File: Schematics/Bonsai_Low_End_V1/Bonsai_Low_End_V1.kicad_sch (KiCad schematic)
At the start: 6 parts, among them U1 MOUDLE-SEEEDUINO-XIAO-ESP32C3, U2 MAX30101EFD

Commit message: Before Everything Breaks
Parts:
- removed C2: 10uF, symbol Device:C_Small
- added C3: 1.0uF, symbol Device:C_Small
- added C5: 10uF, symbol Device:C_Small
- added D1: RED, symbol Device:LED
- added J1: Conn_01x02_Socket, symbol Connector:Conn_01x02_Socket
- added R3: 2,2k, symbol Device:R_Small
- added R4, R7, R8: 4.7k, symbol Device:R_Small
- added R4, R5, R6: 2.2k, symbol Device:R_Small
- added U3, U4: RE1C002UN, RE1C002UN:EMT3F, symbol RE1C002UN:RE1C002UN
- added U5: DRV2605LDGS, Package_SO:VSSOP-10_3x3mm_P0.5mm, symbol Driver_Haptic:DRV2605LDGS
- U1: footprint MOUDLE14P-SMD-2.54-21X17.8MM -> xiao ESP32C3_PCB:MOUDLE14P-SMD-2.54-21X17.8MM
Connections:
- net GND2 is gone; now on net GND: U2.4 (PGND)
- net +1V8: now also R1.1, R3.1, U3.P$1, U4.P$1
- net +5V: now also C5.1
- net GND: now also U1.13 (GND), C3.2, C5.2, R7.2, R8.2, U5.4 (IN/TRIG), U5.8 (GND)
- net LV_SCL: now also R1.2, U3.P$2
- net LV_SDA: now also R3.2, U4.P$2
- net SCL: now also R2.2, U1.6 (PA9_A5_D5_SCL), R6.1, U3.P$3, U5.2 (SCL); no longer U1.5 (PA8_A4_D4_SDA)
- net SDA: now also U1.5 (PA8_A4_D4_SDA), R4.2, R5.1, U4.P$3, U5.3 (SDA); no longer U1.6 (PA9_A5_D5_SCL)
- net +3V3: now reaches R2.1
- net +3V3: now also U1.12 (3V3), R4.1, R4.1, R5.2, R6.2
- net HapticEN: now reaches U1.10 (PA5_A9_D9_MISO)
- net HapticEN: now also R8.1, U5.5 (EN)
- net at U1.11 (PA6_A10_D10_MOSI): now also D1.2 (A)
- net VCC: now reaches U1.14 (5V)
- net VCC: now also U5.10 (VDD), U5.6 (VDD/NC)
- net !INT: no longer names the net of U2.13 (~{INT})
- net !INT: now also R4.2
- new net: D1.1 (K), R7.1
- new net: C3.1, U5.1 (REG)
- new net: J1.1 (Pin_1), U5.7 (OUT+)
- new net: J1.2 (Pin_2), U5.9 (OUT-)
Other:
- moved on the sheet: C1, R1, R2, U1, U2

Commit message: Added Driver and Haptic Motor
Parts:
- removed J1: Conn_01x02_Socket, symbol Connector:Conn_01x02_Socket
- removed R4: 4.7k, symbol Device:R_Small
- added R9: 2.2k, symbol Device:R_Small
- added U6: ~, BonsaiFootPrintLib:VLV101040A, symbol Custom_Symbols_Bonsai:VLV101040A
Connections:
- net +3V3: now also R9.1
- net at U5.7 (OUT+): now also U6.1 (VCC)
- net at U5.9 (OUT-): now also U6.2 (GND)
- net at U2.13 (~{INT}): now also R9.2
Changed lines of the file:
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@@
+    (effects (font (size 1.27 1.27)) (justify left bottom))
+  )
+  (label "Driver and Haptic Motor" (at 142.24 81.28 0) (fields_autoplaced)
     (effects (font (size 1.27 1.27)) (justify left bottom))
   )
@@
     )
   )
+  (symbol (lib_id "Custom_Symbols_Bonsai:VLV101040A") (at 185.42 99.06 0) (unit 1)
+    (in_bom yes) (on_board yes) (dnp no) (fields_autoplaced)
+    (property "Reference" "U6" (at 189.23 100.33 0)
+      (effects (font (size 1.27 1.27)) (justify left))
+    )
+    (property "Value" "~" (at 185.42 99.06 0)
+      (effects (font (size 1.27 1.27)))
+    )
+    (property "Footprint" "BonsaiFootPrintLib:VLV101040A" (at 185.42 99.06 0)
+      (effects (font (size 1.27 1.27)) hide)
+    )
+    (property "Datasheet" "" (at 185.42 99.06 0)
+      (effects (font (size 1.27 1.27)) hide)
+    )
+    (pin "1")
+    (pin "2")
+    (instances
+      (project "Bonsai_Low_End_V1"
+        (path "/b393c629-c38d-42fe-a79b-f8ec17a7bd02"
+          (reference "U6") (unit 1)
+        )
+      )
+    )
+  )
   (symbol (lib_id "Device:R_Small") (at 152.4 118.11 0) (unit 1)
     (in_bom yes) (on_board yes) (dnp no)
@@
     )
   )
-  (symbol (lib_id "Connector:Conn_01x02_Socket") (at 189.23 95.25 0) (unit 1)
-    (in_bom yes) (on_board yes) (dnp no)
-    (property "Reference" "J1" (at 190.5 90.17 0)
-      (effects (font (size 1.27 1.27)) (justify left))
-    )
-    (property "Value" "Conn_01x02_Socket" (at 190.5 92.71 0)
-      (effects (font (size 1.27 1.27)) (justify left))
-    )
-    (property "Footprint" "" (at 189.23 95.25 0)
-      (effects (font (size 1.27 1.27)) hide)
-    )
-    (property "Datasheet" "~" (at 189.23 95.25 0)
-      (effects (font (size 1.27 1.27)) hide)
-    )
-    (pin "1")
-    (pin "2")
-    (instances
-      (project "Bonsai_Low_End_V1"
-        (path "/b393c629-c38d-42fe-a79b-f8ec17a7bd02"
-          (reference "J1") (unit 1)
-        )
-      )
-    )
-  )
   (symbol (lib_id "power:+5V") (at 151.13 44.45 0) (unit 1)
     (in_bom yes) (on_board yes) (dnp no)
@@
         (path "/b393c629-c38d-42fe-a79b-f8ec17a7bd02"
           (reference "#PWR011") (unit 1)
-        )
-      )
-    )
-  )
-  (symbol (lib_id "Device:R_Small") (at 184.15 22.86 0) (unit 1)
-    (in_bom yes) (on_board yes) (dnp no) (fields_autoplaced)
-    (property "Reference" "R4" (at 186.69 21.59 0)
-      (effects (font (size 1.27 1.27)) (justify left))
-    )
-    (property "Value" "4.7k" (at 186.69 24.13 0)
-      (effects (font (size 1.27 1.27)) (justify left))
-    )
-    (property "Footprint" "" (at 184.15 22.86 0)
-      (effects (font (size 1.27 1.27)) hide)
-    )
-    (property "Datasheet" "~" (at 184.15 22.86 0)
-      (effects (font (size 1.27 1.27)) hide)
-    )
-    (pin "1")
-    (pin "2")
-    (instances
-      (project "Bonsai_Low_End_V1"
-        (path "/b393c629-c38d-42fe-a79b-f8ec17a7bd02"
-          (reference "R4") (unit 1)
         )
       )
@@
         )
       )
+    )
+  )
+  (symbol (lib_id "Device:R_Small") (at 184.15 22.86 0) (unit 1)
+    (in_bom yes) (on_board yes) (dnp no) (fields_autoplaced)
+    (property "Reference" "R9" (at 186.69 21.59 0)
+      (effects (font (size 1.27 1.27)) (justify left))
+    )
+    (property "Value" "2.2k" (at 186.69 24.13 0)
+      (effects (font (size 1.27 1.27)) (justify left))
+    )
+    (property "Footprint" "" (at 184.15 22.86 0)
+      (effects (font (size 1.27 1.27)) hide)
+    )
+    (property "Datasheet" "~" (at 184.15 22.86 0)
+      (effects (font (size 1.27 1.27)) hide)
+    )
+    (pin "1")
+    (pin "2")
+    (instances
+      (project "Bonsai_Low_End_V1"
+        (path "/b393c629-c38d-42fe-a79b-f8ec17a7bd02"
+          (reference "R9") (unit 1)
+        )
+      )

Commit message: last psuh before feedback
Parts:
- removed R3: 2,2k, symbol Device:R_Small
- removed R4: 2.2k, symbol Device:R_Small
- removed U4: RE1C002UN, RE1C002UN:EMT3F, symbol RE1C002UN:RE1C002UN
- added U7: RE1C002UN, RE1C002UN:EMT3F, symbol RE1C002UN:RE1C002UN
- C5: value 10uF -> 50uF
- R2: value 2.2k -> 2,2k
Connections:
- net +1V8: now also R2.1, U7.P$1
- net +3V3: no longer R2.1
- net +5V: no longer C5.1
- net LV_SDA: now also R2.2, U7.P$2
- net SCL: no longer R2.2
- net SDA: now also U7.P$3
- net VCC: now also C5.1
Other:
- company: (none) -> Bonsai
- title: (none) -> Bonsai Wearable Prototype
- moved on the sheet: C1, C3, C5, D1, R1, R5, R6, R7, R8, R9, U1, U2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

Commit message: Made PCB
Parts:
- C1, C3: footprint (none) -> Capacitor_SMD:C_0603_1608Metric_Pad1.08x0.95mm_HandSolder
- C5: footprint (none) -> Capacitor_SMD:C_0805_2012Metric_Pad1.18x1.45mm_HandSolder
- D1: footprint (none) -> LED_SMD:LED_0603_1608Metric_Pad1.05x0.95mm_HandSolder
- R1, R2, R5, R6, R7, R8, R9: footprint (none) -> Resistor_SMD:R_0603_1608Metric_Pad0.98x0.95mm_HandSolder
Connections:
- net HapticEN: now also U1.3 (PA10_A2_D2); no longer U1.10 (PA5_A9_D9_MISO)
- net at U1.11 (PA6_A10_D10_MOSI): no longer D1.2 (A)
- net FUN_LIGHT: now reaches U1.7 (PB08_A6_D6_TX)
- net FUN_LIGHT: now also D1.2 (A)
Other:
- moved on the sheet: C1, C3, C5, D1, R1, R2, R5, R6, R7, R8, R9, U1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

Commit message: Improved
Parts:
- removed U3, U7: RE1C002UN, RE1C002UN:EMT3F, symbol RE1C002UN:RE1C002UN
- added C2: 1uF, Capacitor_SMD:C_0805_2012Metric_Pad1.18x1.45mm_HandSolder, symbol Device:C_Small
- added D2: D_Small_Filled, symbol Device:D_Small_Filled
- added J1: Bat_Connector, Connector_JST:JST_EH_B2B-EH-A_1x02_P2.50mm_Vertical, symbol PCM_SL_Connectors:JST_02
- added Q1: PMOS, symbol Simulation_SPICE:PMOS
- added R3: 2.2k, Resistor_SMD:R_0603_1608Metric_Pad0.98x0.95mm_HandSolder, symbol Device:R_Small
- added R4: 4.7k, Resistor_SMD:R_0603_1608Metric_Pad0.98x0.95mm_HandSolder, symbol Device:R_Small
- added U3: 1.8V, Package_TO_SOT_SMD:SOT-23-5, symbol Regulator_Linear:AP2204K-1.8
- R1: value 2,2k -> 4.7k
- R2: value 2,2k -> 2.2k
- R5: value 2.2k -> 4.7k
- R6, R9: value 2.2k -> 220k
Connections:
- net +5V is gone; now on net VCC: U2.10 (VLED+), U2.9 (VLED+)
- net +1V8: now also U3.5 (VOUT); no longer R1.1, R2.1
- net +3V3: now also R2.2, R3.2; no longer R5.2, R6.2, R9.1
- net GND: now also R1.2, R5.2, C2.2, U3.2 (GND); no longer U5.4 (IN/TRIG)
- net HapticEN: now also U1.2 (PA4_A1_D1); no longer U1.3 (PA10_A2_D2)
- net SCL: now also U2.2 (SCL), R3.1; no longer R6.1
- net SDA: now also R2.1, U2.3 (SDA); no longer R5.1
- net VCC: now also C2.1, R4.2, U3.1 (VIN)
- net Bat_Ind: now reaches R9.2
- net Bat_Ind: now also U1.11 (PA6_A10_D10_MOSI), Q1.1 (D); no longer U2.13 (~{INT})
- net DRV_IN/TRIG: now reaches U1.10 (PA5_A9_D9_MISO)
- net DRV_IN/TRIG: now also R5.1, U5.4 (IN/TRIG)
- net Bat_Ind_EN: now reaches U1.4 (PA11_A3_D3)
- net Bat_Ind_EN: now also Q1.2 (G)
- net INT MAX: now reaches U1.8 (PB09_A7_D7_RX)
- net INT MAX: now also U2.13 (~{INT}), R4.1
- removed net LV_SCL: R1.2, U2.2 (SCL)
- removed net LV_SDA: R2.2, U2.3 (SDA)
- new net: Q1.3 (S), R6.2
- new net: R1.1, U3.3 (EN)
- new net: D2.2 (A), J1.1
- new net Bat+: D2.1 (K), R6.1, U1.15 (Bat+)
- new net Bat-: J1.2, R9.1, U1.16 (Bat-)
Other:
- note added: "Battery Stuff"
- note added: "NOT TO BE USED AS VCC!"
- moved on the sheet: C3, C5, D1, R7, R8, U2, U5, U6

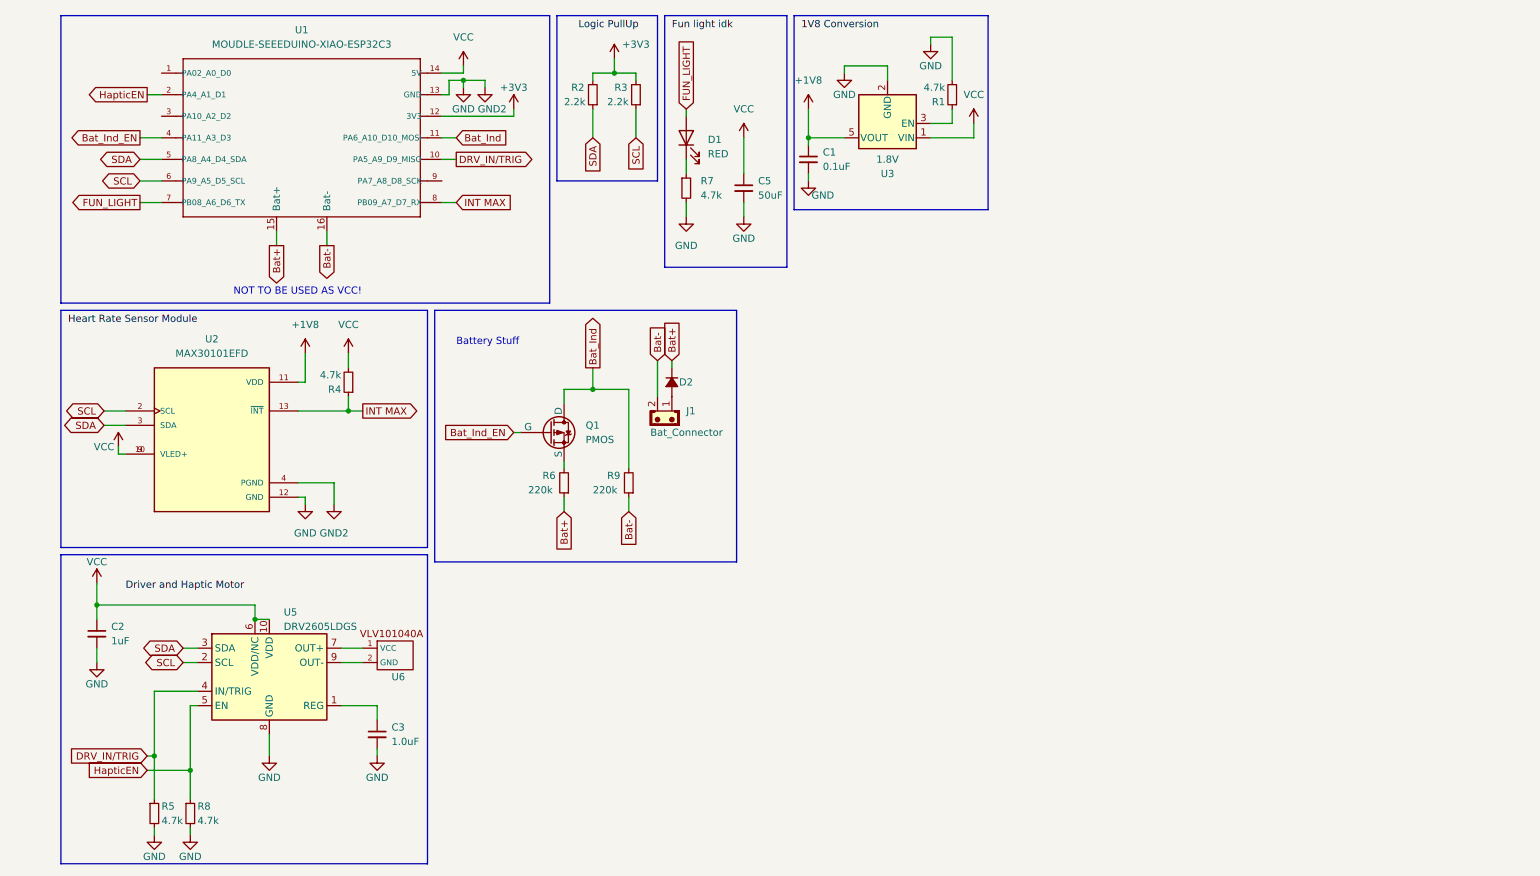
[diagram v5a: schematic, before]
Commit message: fixed orientation of nmos
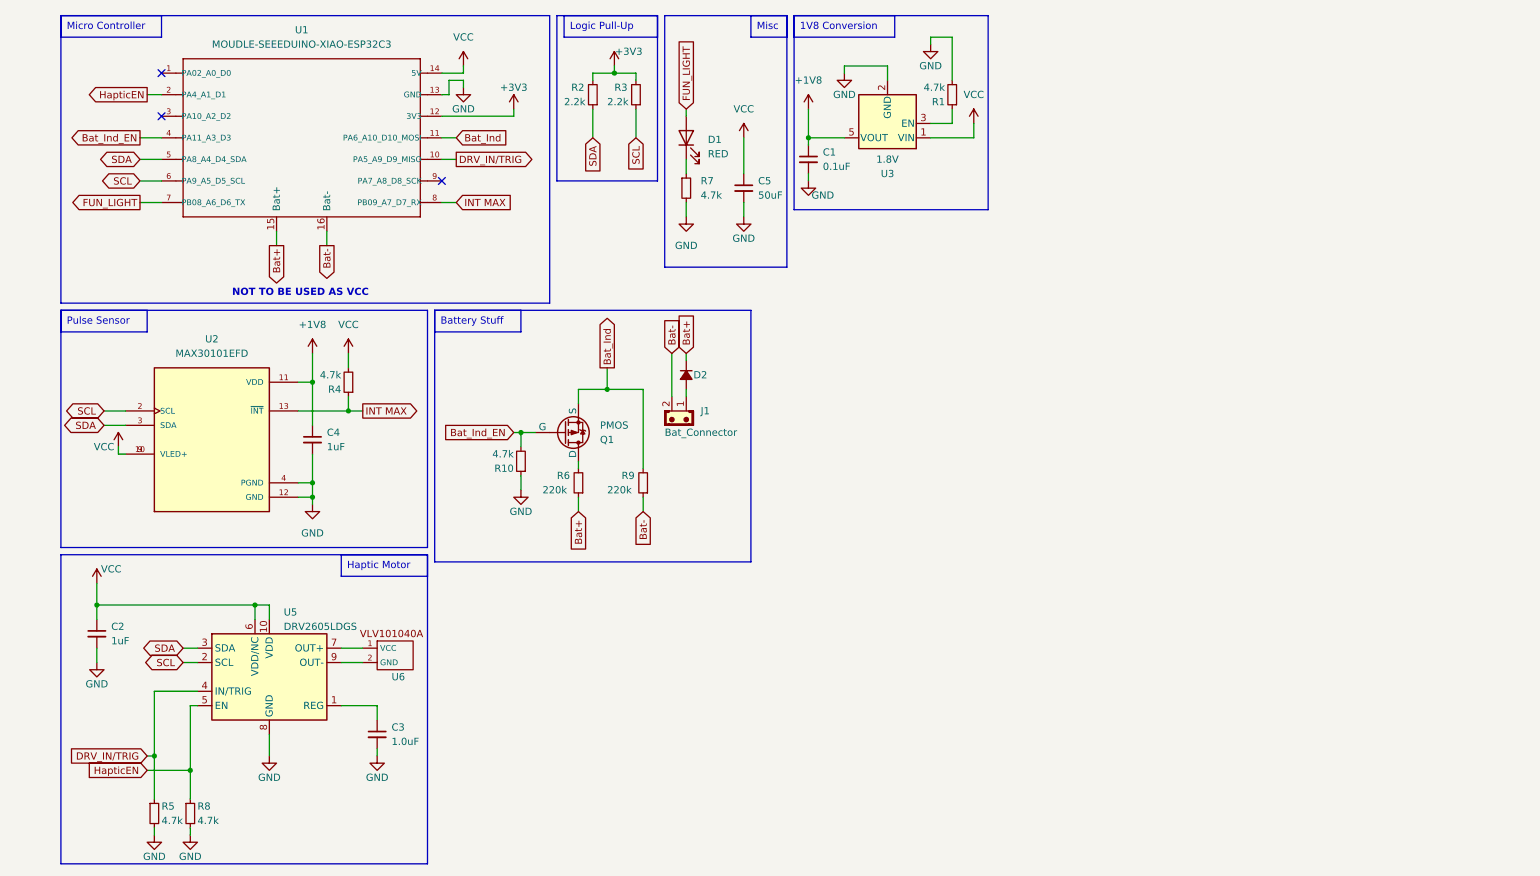
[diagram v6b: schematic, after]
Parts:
- added C4: 1uF, Capacitor_SMD:C_0805_2012Metric_Pad1.18x1.45mm_HandSolder, symbol Device:C_Small
- added R10: 4.7k, Resistor_SMD:R_0603_1608Metric_Pad0.98x0.95mm_HandSolder, symbol Device:R_Small
- D2: footprint (none) -> Diode_SMD:D_0603_1608Metric_Pad1.05x0.95mm_HandSolder
- J1: footprint Connector_JST:JST_EH_B2B-EH-A_1x02_P2.50mm_Vertical -> Connector_JST:JST_SH_SM02B-SRSS-TB_1x02-1MP_P1.00mm_Horizontal
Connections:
- net +1V8: now also C4.1
- net Bat_Ind: now also Q1.3 (S); no longer Q1.1 (D)
- net Bat_Ind_EN: now also R10.2
- net GND: now also C4.2, R10.1
- net at R6.2: now also Q1.1 (D); no longer Q1.3 (S)
- no-connect marks 0 -> 3
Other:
- note removed: "Battery Stuff"
- note removed: "NOT TO BE USED AS VCC!"
- moved on the sheet: D2, J1, Q1, R6, R9

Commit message: prior disaster
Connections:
- net Bat-: now also R10.1
- net GND: no longer R10.1
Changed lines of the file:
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@@
   (junction (at 118.11 24.13) (diameter 0) (color 0 0 0 0)
+  )
+  (junction (at 123.19 100.33) (diameter 0) (color 0 0 0 0)
   )
   (junction (at 71.12 83.82) (diameter 0) (color 0 0 0 0)
@@
     (stroke (width 0) (type default))
   )
-  (wire (pts (xy 101.6 95.25) (xy 101.6 97.79))
+  (wire (pts (xy 101.6 100.33) (xy 123.19 100.33))
     (stroke (width 0) (type default))
   )
@@
     (stroke (width 0) (type default))
   )
-  (wire (pts (xy 123.19 99.06) (xy 123.19 101.6))
+  (wire (pts (xy 123.19 99.06) (xy 123.19 100.33))
     (stroke (width 0) (type default))
   )
@@
     (stroke (width 0) (type default))
   )
+  (wire (pts (xy 101.6 95.25) (xy 101.6 100.33))
+    (stroke (width 0) (type default))
+  )
   (wire (pts (xy 123.19 80.01) (xy 116.84 80.01))
     (stroke (width 0) (type default))
@@
   )
   (wire (pts (xy 64.77 91.44) (xy 64.77 96.52))
+    (stroke (width 0) (type default))
+  )
+  (wire (pts (xy 123.19 100.33) (xy 123.19 101.6))
     (stroke (width 0) (type default))
   )
@@
     )
   )
-  (symbol (lib_id "power:GND") (at 101.6 97.79 0) (unit 1)
-    (in_bom yes) (on_board yes) (dnp no)
-    (property "Reference" "#PWR06" (at 101.6 104.14 0)
-      (effects (font (size 1.27 1.27)) hide)
-    )
-    (property "Value" "GND" (at 101.6 101.6 0)
-      (effects (font (size 1.27 1.27)))
-    )
-    (property "Footprint" "" (at 101.6 97.79 0)
-      (effects (font (size 1.27 1.27)) hide)
-    )
-    (property "Datasheet" "" (at 101.6 97.79 0)
-      (effects (font (size 1.27 1.27)) hide)
-    )
-    (pin "1")
-    (instances
-      (project "Bonsai_Low_End_V1"
-        (path "/b393c629-c38d-42fe-a79b-f8ec17a7bd02"
-          (reference "#PWR06") (unit 1)
-        )
-      )
-    )
-  )
   (symbol (lib_id "MOUDLE-SEEEDUINO-XIAO-ESP32C3:MOUDLE-SEEEDUINO-XIAO-ESP32C3") (at 63.5 35.56 0) (unit 1)
     (in_bom yes) (on_board yes) (dnp no) (fields_autoplaced)
@@
     (pin "10")
     (pin "11")
-    (pin "13")
     (pin "14")
     (pin "2")
@@
     (pin "9")
     (pin "12")
+    (pin "13")
     (pin "15")
     (pin "16")

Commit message: prior symbol change
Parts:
- removed Q1: PMOS, symbol Simulation_SPICE:PMOS
- removed R10: 4.7k, Resistor_SMD:R_0603_1608Metric_Pad0.98x0.95mm_HandSolder, symbol Device:R_Small
- added C6: 8nF, Capacitor_SMD:C_0805_2012Metric_Pad1.18x1.45mm_HandSolder, symbol Device:C_Small
- R6: value 220k -> 4M
- R9: value 220k -> 10M
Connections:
- net Bat+: now also R6.2; no longer R6.1
- net Bat-: now also C6.2
- net Bat_Ind: now also R6.1, C6.1
- net Bat_Ind_EN: no longer names the net of U1.4 (PA11_A3_D3)
- no-connect marks 3 -> 4
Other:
- moved on the sheet: C1, C2, C3, C4, C5, D1, D2, J1, R1, R2, R3, R4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
